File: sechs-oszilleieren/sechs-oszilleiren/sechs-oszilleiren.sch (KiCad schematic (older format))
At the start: 3 parts

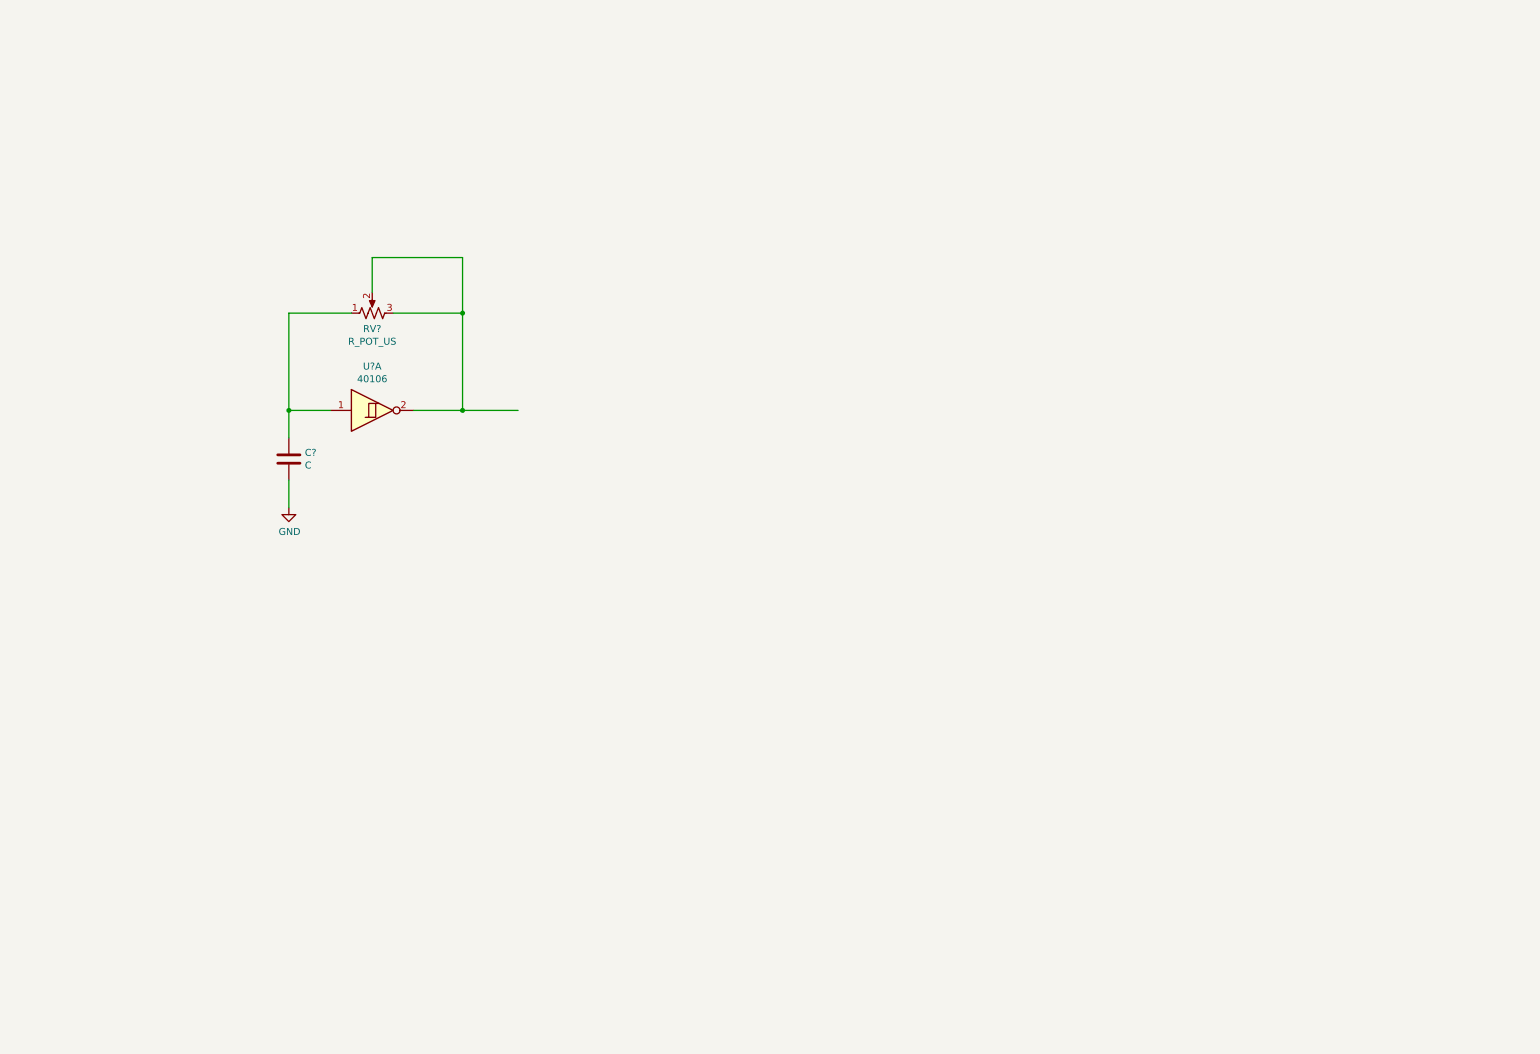
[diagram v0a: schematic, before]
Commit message: Added the remaining segments as well as a mixing output stage and indicator lights.
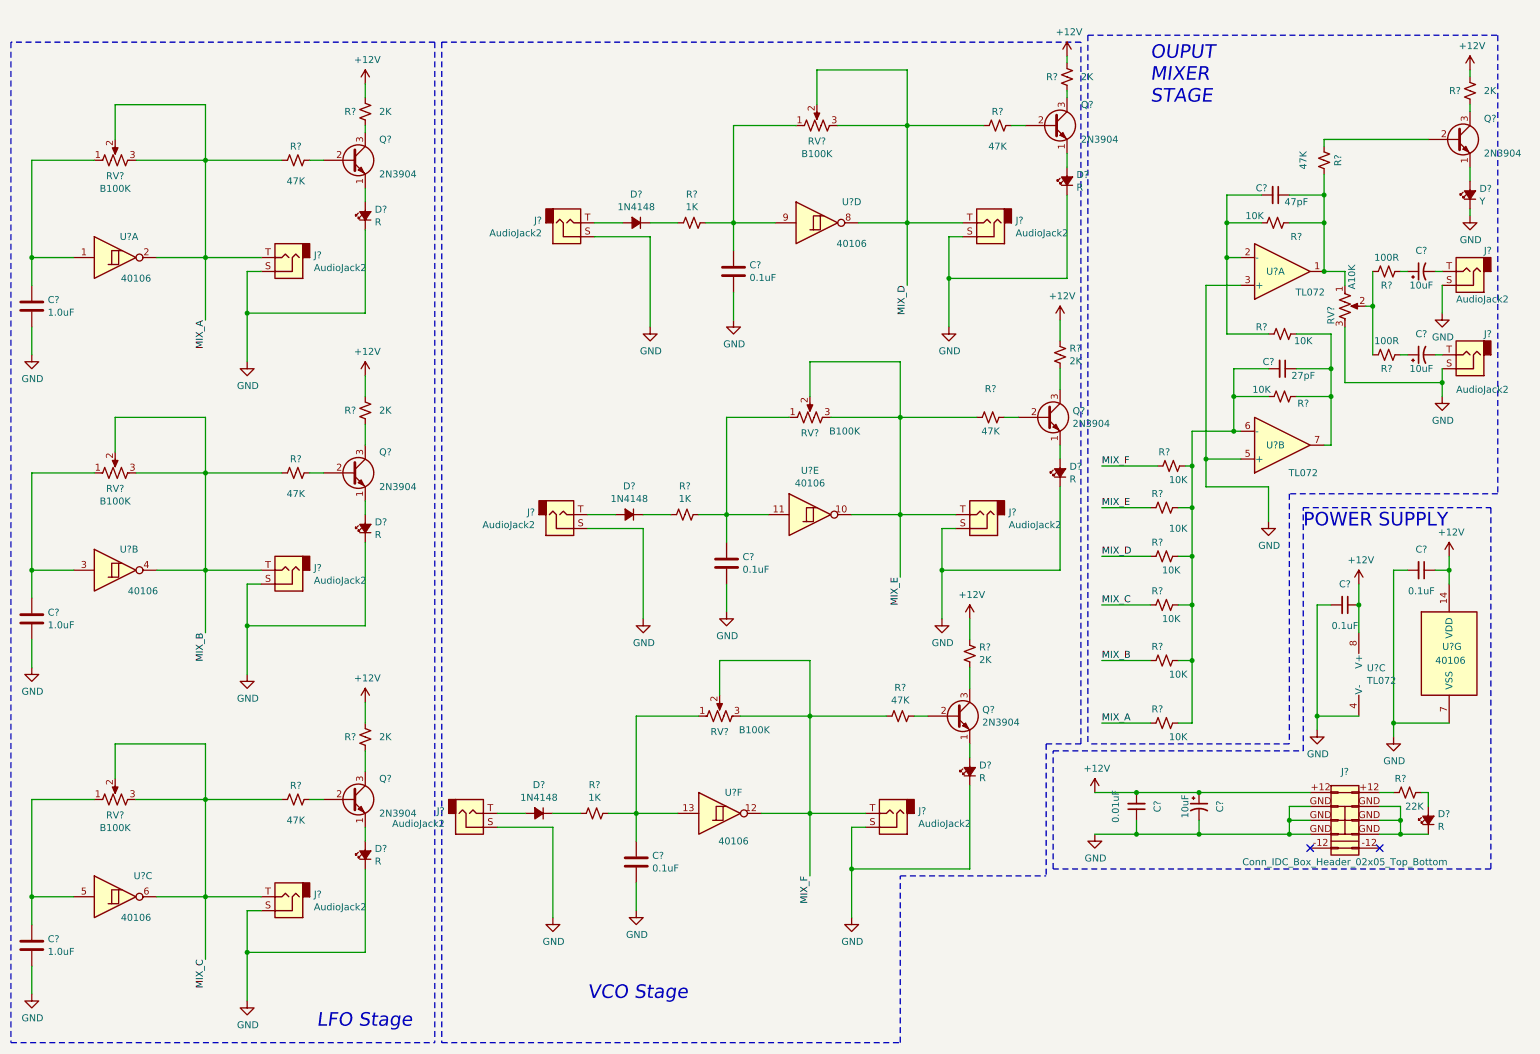
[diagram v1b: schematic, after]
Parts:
- added C? (x2): 1.0uF, symbol Device:C
- added C? (x3): 0.1uF, symbol Device:C
- added C? (x2): 0.1uF, symbol Device:C_Small
- added C? (x3): 10uF, symbol Device:CP1_Small
- added C?: 0.01uF, symbol Device:C_Small
- added C?: 47pF, symbol Device:C_Small
- added C?: 27pF, symbol Device:C_Small
- added D? (x3): 1N4148, symbol Device:D_Small_ALT
- added D? (x7): R, symbol Device:LED_Small_ALT
- added D?: Y, symbol Device:LED_Small_ALT
- added J? (x11): AudioJack2, symbol Connector:AudioJack2
- added J?: Conn_IDC_Box_Header_02x05_Top_Bottom, symbol Conn_IDC_Eurorack:Conn_IDC_Box_Header_02x05_Top_Bottom
- added Q? (x7): 2N3904, Package_TO_SOT_THT:TO-92_Inline, symbol Transistor_BJT:2N3904
- added R? (x3): 1K, symbol Device:R_Small_US
- added R? (x7): 2K, symbol Device:R_Small_US
- added R? (x7): 47K, symbol Device:R_Small_US
- added R?: 22K, symbol Device:R_Small_US
- added R? (x2): 100R, symbol Device:R_Small_US
- added R? (x9): 10K, symbol Device:R_Small_US
- added RV? (x5): B100K, symbol Device:R_POT_US
- added RV?: A10K, symbol Device:R_POT_US
- added U? (x6): 40106, symbol 4xxx:40106
- added U? (x3): TL072, symbol Amplifier_Operational:TL072
- C?: value C -> 1.0uF
- RV?: value R_POT_US -> B100K
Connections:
- net labels added: +12V, MIX_A, MIX_B, MIX_C, MIX_D, MIX_E, MIX_F
- wire segments 12 -> 257
- no-connect marks 0 -> 2
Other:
- note added: "LFO Stage"
- note added: "OUPUT \nMIXER \nSTAGE"
- note added: "POWER SUPPLY"
- note added: "VCO Stage"
- moved on the sheet: C?, RV?, U?A

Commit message: Added nearly all parts and wires. Some are being stubborn and will need some revision.
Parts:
- C101, C102, C103, C104, C105, C106, C107, C109, C110, C111, C114: renamed from C?; footprint (none) -> Capacitor_SMD:C_0805_2012Metric
- C108, C112, C113: renamed from C?; footprint (none) -> Capacitor_SMD:CP_Elec_5x5.4
- D101, D102, D103, D107, D108, D109, D110, D111: renamed from D?; footprint (none) -> LED_THT:LED_D3.0mm
- D104, D105, D106: renamed from D?; footprint (none) -> Diode_SMD:D_SOD-323
- J101, J102, J103, J104, J105, J106, J107, J108, J109, J111, J112: renamed from J?; footprint (none) -> Connector_Audio:Jack_3.5mm_QingPu_WQP-PJ398SM_Vertical_CircularHoles
- J110: renamed from J?; footprint (none) -> Connectors_IDC:IDC-Header_2x05_Pitch2.54mm_Straight
- Q101, Q102, Q103, Q104, Q105, Q106, Q107: renamed from Q?; footprint Package_TO_SOT_THT:TO-92_Inline -> Package_TO_SOT_SMD:SOT-23
- R101, R102, R103, R104, R105, R106, R107, R108, R109, R110, R111, R112, R113, R114, R115, R116, R117, R118, R119, R120, R121, R122, R123, R124, R125, R126, R127, R128, R129: renamed from R?; footprint (none) -> Resistor_SMD:R_0805_2012Metric
- RV101, RV102, RV103, RV104, RV105, RV106, RV107: renamed from RV?; footprint (none) -> Potentiometer_THT:Potentiometer_Alpha_RD901F-40-00D_Single_Vertical_CircularHoles
- U101: renamed from U?; footprint (none) -> Package_SO:SOIC-14_3.9x8.7mm_P1.27mm
- U102: renamed from U?; footprint (none) -> Package_SO:SOIC-8_3.9x4.9mm_P1.27mm
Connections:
- net GND: now also D110.1 (K)
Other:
- note added: "LEVEL"
- moved on the sheet: C105, C106, D105, D106, D108, D109, J105, J106, J108, J109, Q105, Q106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

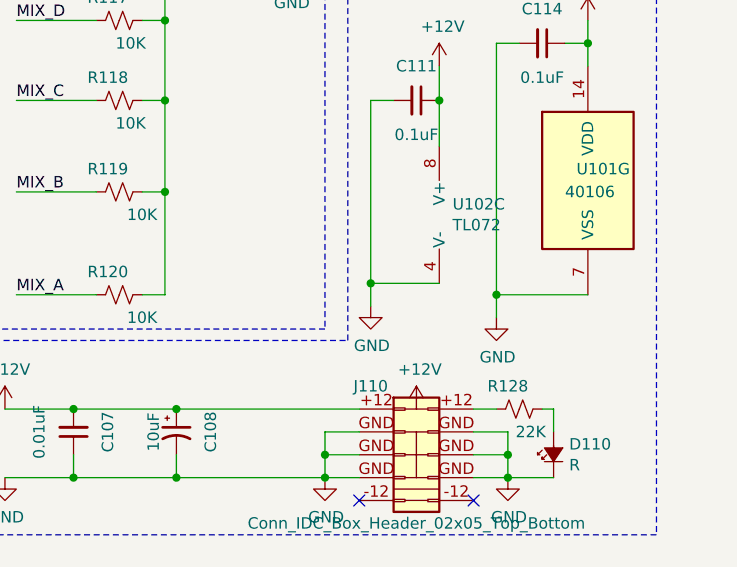
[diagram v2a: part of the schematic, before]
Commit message: Started rearranging the components on the boards such that a panel may also be laid out in FR4
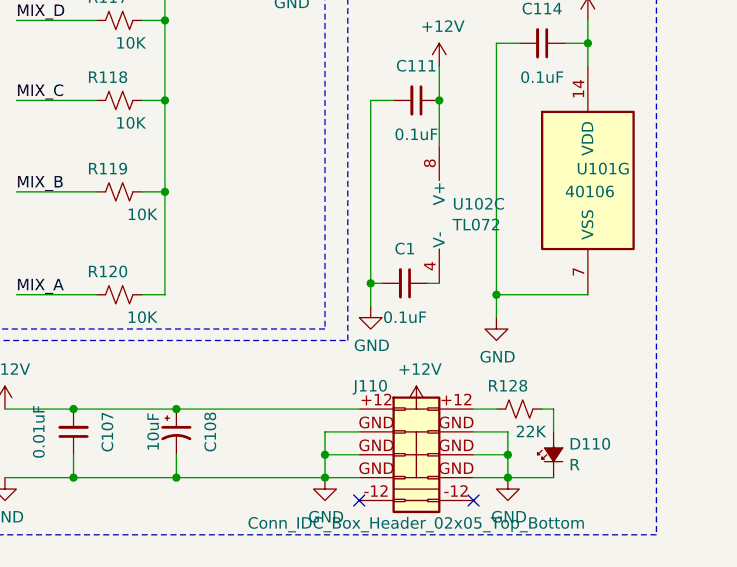
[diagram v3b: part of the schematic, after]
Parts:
- added C1: 0.1uF, Capacitor_SMD:C_0805_2012Metric, symbol Device:C_Small
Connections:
- net GND: now also C1.2; no longer U102.4 (V-)
- new net: C1.1, U102.4 (V-)
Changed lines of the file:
@@
 $EndComp
 Wire Wire Line
-	10200 5400 9900 5400
+	10200 5400 10150 5400
 Connection ~ 9900 5400
 Wire Wire Line
@@
 	1    0    0    -1
 $EndComp
+$Comp
+L Device:C_Small C1
+U 1 1 5E67B3D2
+P 10050 5400
+F 0 "C1" V 9900 5400 50  0000 C CNN
+F 1 "0.1uF" V 10200 5400 50  0000 C CNN
+F 2 "Capacitor_SMD:C_0805_2012Metric" H 10050 5400 50  0001 C CNN
+F 3 "~" H 10050 5400 50  0001 C CNN
+	1    10050 5400
+	0    1    1    0
+$EndComp
+Wire Wire Line
+	9950 5400 9900 5400
 $EndSCHEMATC

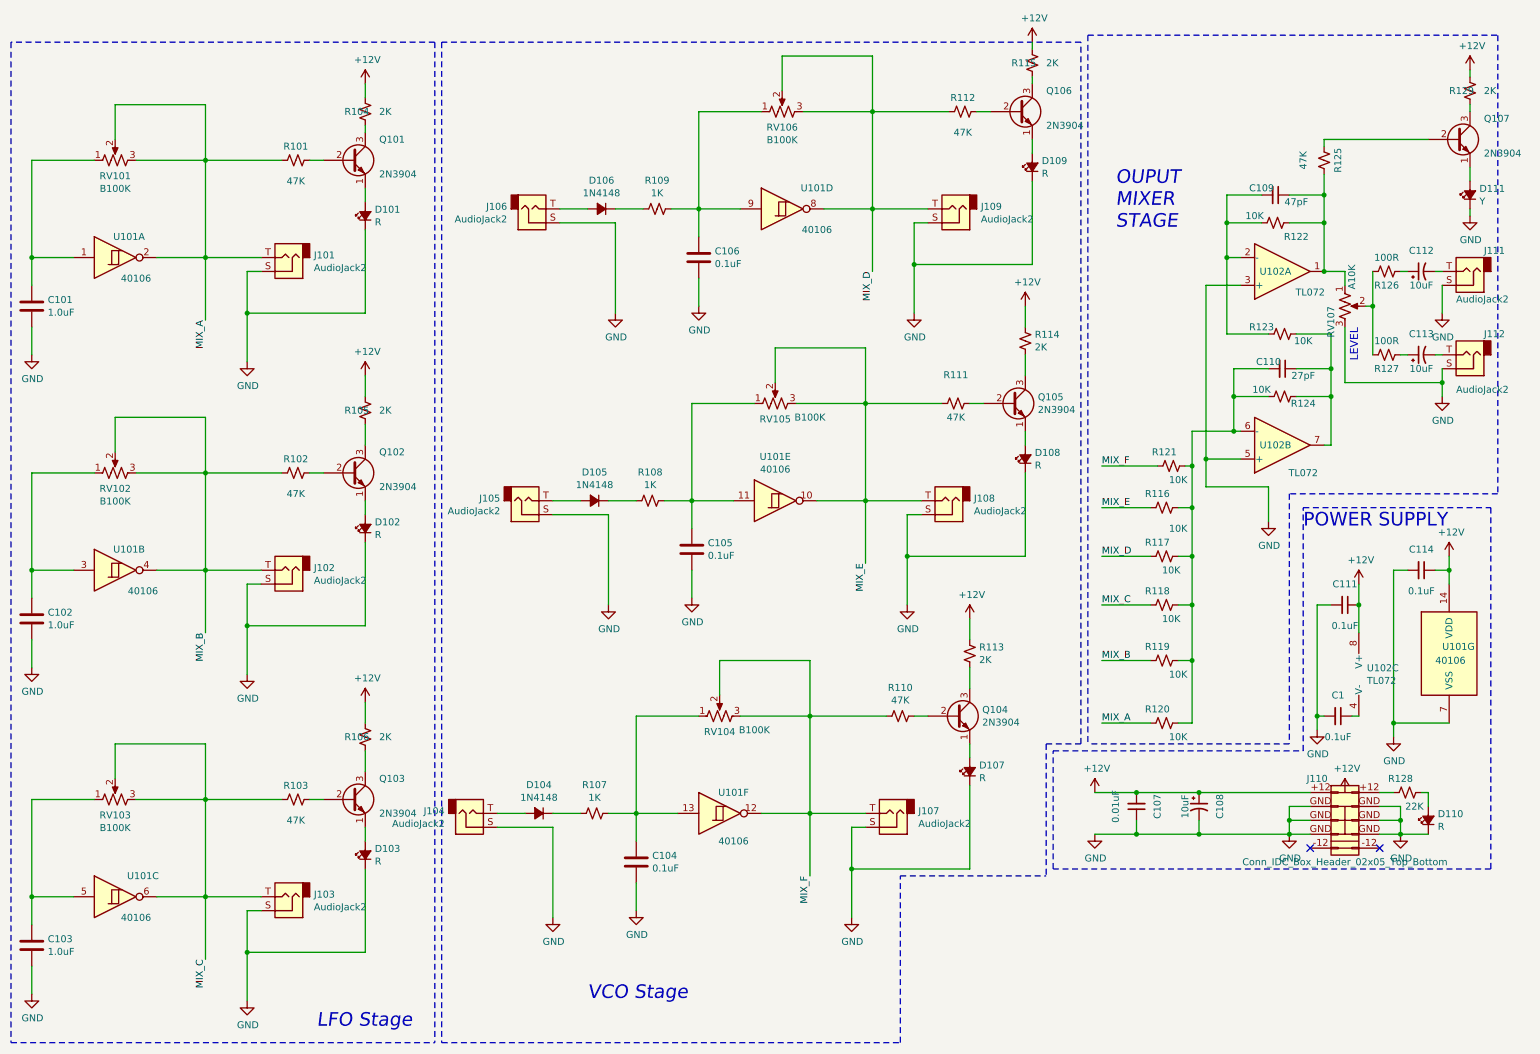
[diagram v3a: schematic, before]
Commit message: Added pins between boards for stacking. Changed all components to THT components.
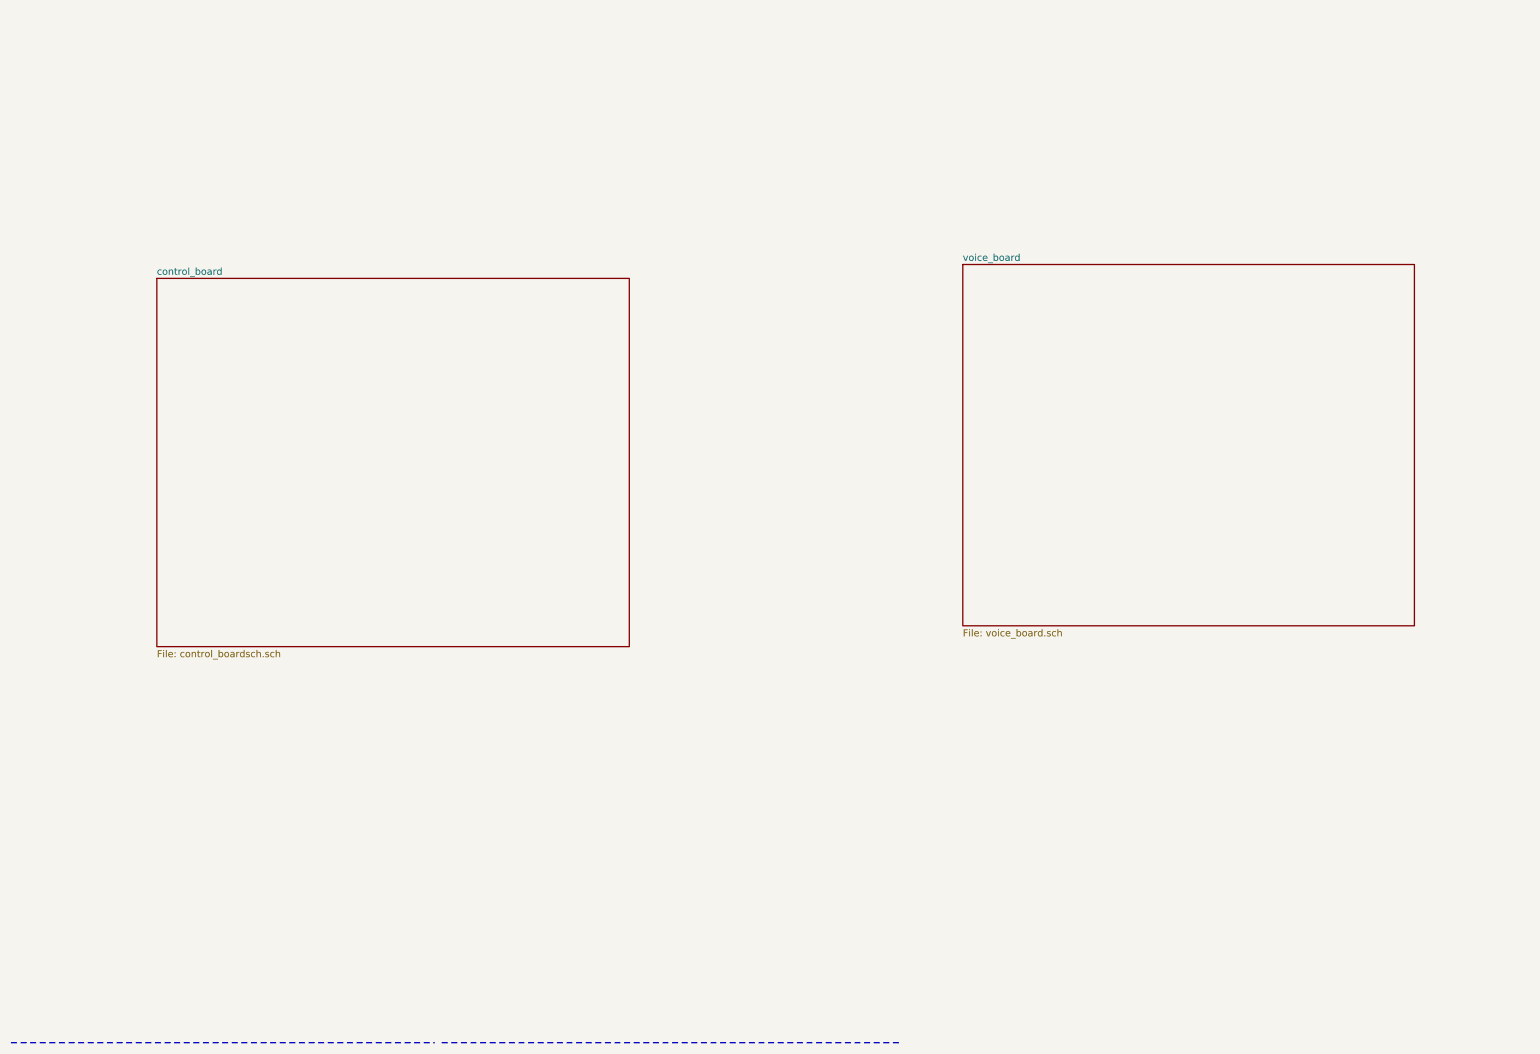
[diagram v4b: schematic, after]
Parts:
- removed C1, C111, C114: 0.1uF, Capacitor_SMD:C_0805_2012Metric, symbol Device:C_Small
- removed C101, C102, C103: 1.0uF, Capacitor_SMD:C_0805_2012Metric, symbol Device:C
- removed C104, C105, C106: 0.1uF, Capacitor_SMD:C_0805_2012Metric, symbol Device:C
- removed C107: 0.01uF, Capacitor_SMD:C_0805_2012Metric, symbol Device:C_Small
- removed C108, C112, C113: 10uF, Capacitor_SMD:CP_Elec_5x5.4, symbol Device:CP1_Small
- removed C109: 47pF, Capacitor_SMD:C_0805_2012Metric, symbol Device:C_Small
- removed C110: 27pF, Capacitor_SMD:C_0805_2012Metric, symbol Device:C_Small
- removed D101, D102, D103, D107, D108, D109, D110: R, LED_THT:LED_D3.0mm, symbol Device:LED_Small_ALT
- removed D104, D105, D106: 1N4148, Diode_SMD:D_SOD-323, symbol Device:D_Small_ALT
- removed D111: Y, LED_THT:LED_D3.0mm, symbol Device:LED_Small_ALT
- removed J101, J102, J103, J104, J105, J106, J107, J108, J109, J111, J112: AudioJack2, Connector_Audio:Jack_3.5mm_QingPu_WQP-PJ398SM_Vertical_CircularHoles, symbol Connector:AudioJack2
- removed J110: Conn_IDC_Box_Header_02x05_Top_Bottom, Connectors_IDC:IDC-Header_2x05_Pitch2.54mm_Straight, symbol Conn_IDC_Eurorack:Conn_IDC_Box_Header_02x05_Top_Bottom
- removed Q101, Q102, Q103, Q104, Q105, Q106, Q107: 2N3904, Package_TO_SOT_SMD:SOT-23, symbol Transistor_BJT:2N3904
- removed R101, R102, R103, R110, R111, R112, R125: 47K, Resistor_SMD:R_0805_2012Metric, symbol Device:R_Small_US
- removed R104, R105, R106, R113, R114, R115, R129: 2K, Resistor_SMD:R_0805_2012Metric, symbol Device:R_Small_US
- removed R107, R108, R109: 1K, Resistor_SMD:R_0805_2012Metric, symbol Device:R_Small_US
- removed R116, R117, R118, R119, R120, R121, R122, R123, R124: 10K, Resistor_SMD:R_0805_2012Metric, symbol Device:R_Small_US
- removed R126, R127: 100R, Resistor_SMD:R_0805_2012Metric, symbol Device:R_Small_US
- removed R128: 22K, Resistor_SMD:R_0805_2012Metric, symbol Device:R_Small_US
- removed RV101, RV102, RV103, RV104, RV105, RV106: B100K, Potentiometer_THT:Potentiometer_Alpha_RD901F-40-00D_Single_Vertical_CircularHoles, symbol Device:R_POT_US
- removed RV107: A10K, Potentiometer_THT:Potentiometer_Alpha_RD901F-40-00D_Single_Vertical_CircularHoles, symbol Device:R_POT_US
- removed U101: 40106, Package_SO:SOIC-14_3.9x8.7mm_P1.27mm, symbol 4xxx:40106
- removed U102: TL072, Package_SO:SOIC-8_3.9x4.9mm_P1.27mm, symbol Amplifier_Operational:TL072
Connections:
- no-connect marks 2 -> 0
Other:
- note removed: "LEVEL"
- note removed: "LFO Stage"
- note removed: "OUPUT \nMIXER \nSTAGE"
- note removed: "POWER SUPPLY"
- note removed: "VCO Stage"
